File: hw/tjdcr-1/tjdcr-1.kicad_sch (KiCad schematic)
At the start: 59 parts, among them J1 Conn_Coaxial, J2 Tuning, J3 Power, J4 LO Option, J5 Volume, J6 Power, Q1 MMBT3904, Q2 MMBFJ310, Q3 MMBT3904, Q4 MMBT3904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

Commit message: Layout is progressing
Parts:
- removed Q5: MMBT3904, Package_TO_SOT_SMD:SOT-23, symbol Transistor_BJT:MMBT3904
- added H1, H2, H3, H4: MountingHole, MountingHole:MountingHole_2.5mm, symbol Mechanical:MountingHole
- added Q5: 2N3904, Package_TO_SOT_THT:TO-92_Inline, symbol Transistor_BJT:2N3904
- added TP1, TP2, TP3, TP4: TestPoint, TestPoint:TestPoint_Pad_1.5x1.5mm, symbol Connector:TestPoint
- J1: footprint Connector_Coaxial:SMA_Amphenol_901-143_Horizontal -> Connector_Coaxial:SMA_Amphenol_901-144_Vertical
- J5: footprint (none) -> Connector_PinHeader_2.54mm:PinHeader_1x03_P2.54mm_Vertical
- J6: value Power -> Speaker
- R12: value 10k -> 220
- T5: footprint (none) -> bruce-footprints:CheapAudioTransformer
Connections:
- net Audio: now also TP2.1
- net LO_I: now also TP1.1
- net at C18.2, R20.1: now also Q5.1 (E)
- net at C17.1, R16.2, R18.1: now also Q5.2 (B)
- net at C17.2, Q4.3 (C), R15.2: now also TP3.1
- net at T5.2 (AB): now also Q5.3 (C), TP4.1
- net Speaker Out: now reaches J6.1 (Pin_1), T5.4 (SB)
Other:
- moved on the sheet: J6

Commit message: Working
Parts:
- added C20: 0.47u, Capacitor_SMD:C_0805_2012Metric_Pad1.18x1.45mm_HandSolder, symbol Device:C_Small
- C11: value 0.1u -> 0.33u
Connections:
- net Audio: now also C20.1
- net GND: now also C20.2
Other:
- note added: "40m Band Pass Filter"
- note added: "Audio Diplexer"
- note added: "Audio Power Amplifier"
- note added: "Colpitts PTO/VFO"
- note added: "Connection to external gain pot."
- note added: "Double Balanced Mixer"
- note added: "J2 connection to PTO inductor (19 turns #28 on 3D printed form)"
- note added: "LO option: install jumper across J4 for internal LO, or connect external LO to pin 1 and leave pin 2 open."
- note added: "TO-92 case for better Pd"
- company: (none) -> Circuit Design by N2CQR and KK4DAS
- title: (none) -> Thomas Jefferson Direct Conversion Receiver

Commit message: Checkpoint before adding variable caps
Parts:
- added C21: 0.1u, Capacitor_SMD:C_0805_2012Metric_Pad1.18x1.45mm_HandSolder, symbol Device:C_Small
- added C22, C23: C_Variable, bruce-footprints:VCAP_GKG30086-05_SGM-L, symbol Device:C_Variable
- C11: value 0.33u -> 33u
- C13, C16, C18: footprint Capacitor_Tantalum_SMD:CP_EIA-7343-20_Kemet-V_Pad2.25x2.55mm_HandSolder -> bruce-footprints:CP_EIA-7343
- R20: value 10 -> 100
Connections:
- net GND: now also C21.1, C22.2, C23.2
- net at C2.1, C3.2, T2.4 (SB): now also C23.1
- net at C1.1, C3.1, T1.4 (SB): now also C22.1
- net at Q2.2 (S), R6.1: now also C21.2
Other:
- moved on the sheet: C1, C3, J1, R6, T1

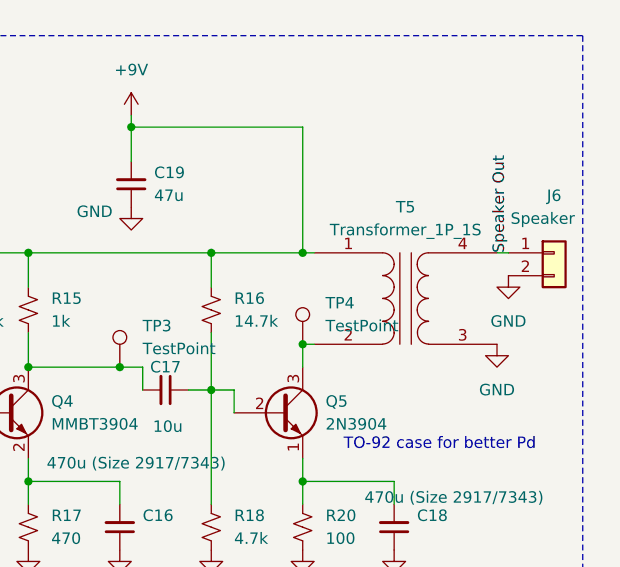
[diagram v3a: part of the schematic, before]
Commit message: Checkpoint after audio transformer change, preparing for flip of audio amp
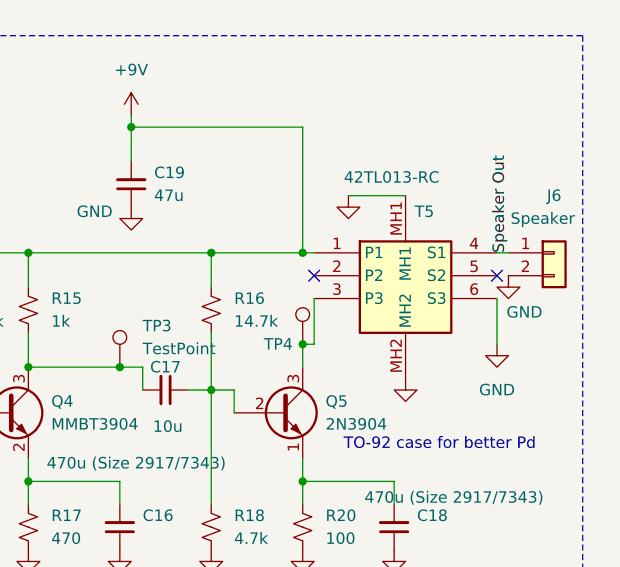
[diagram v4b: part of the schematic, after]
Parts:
- removed T5: Transformer_1P_1S, bruce-footprints:CheapAudioTransformer, symbol Device:Transformer_1P_1S
- added T5: 42TL013-RC, bruce-footprints:42TL013RC, symbol symbol-library-1:42TL013-RC
- J1: footprint Connector_Coaxial:SMA_Amphenol_901-144_Vertical -> Connector_PinHeader_2.54mm:PinHeader_1x02_P2.54mm_Vertical
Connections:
- net +9V: now also T5.1 (P1)
- net GND: now also T5.6 (S3), T5.MH1, T5.MH2
- net Speaker Out: now also T5.4 (S1)
- net at Q5.3 (C), TP4.1: now also T5.3 (P3)
- no-connect marks 0 -> 2

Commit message: Checkpoint after audio amp reverse
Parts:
- added TP5: TestPoint, TestPoint:TestPoint_Pad_1.5x1.5mm, symbol Connector:TestPoint
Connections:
- net at T2.1 (AA), T3.1 (AA): now also TP5.1
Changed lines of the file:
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@@
 	)
 	(junction
+		(at 127 43.18)
+		(diameter 0)
+		(color 0 0 0 0)
+	)
+	(junction
 		(at 210.82 38.1)
 		(diameter 0)
@@
 	(wire
 		(pts
+			(xy 124.46 43.18) (xy 127 43.18)
+		)
+		(stroke
+			(width 0)
+			(type default)
+		)
+	)
+	(wire
+		(pts
 			(xy 227.33 118.11) (xy 227.33 120.65)
 		)
@@
 	(wire
 		(pts
-			(xy 124.46 43.18) (xy 129.54 43.18)
+			(xy 133.35 102.87) (xy 144.78 102.87)
 		)
 		(stroke
@@
 	(wire
 		(pts
-			(xy 133.35 102.87) (xy 144.78 102.87)
+			(xy 144.78 125.73) (xy 144.78 128.27)
 		)
 		(stroke
@@
 	(wire
 		(pts
-			(xy 144.78 125.73) (xy 144.78 128.27)
+			(xy 196.85 43.18) (xy 198.12 43.18)
 		)
 		(stroke
@@
 	(wire
 		(pts
-			(xy 196.85 43.18) (xy 198.12 43.18)
+			(xy 85.09 105.41) (xy 88.9 105.41)
 		)
 		(stroke
@@
 	(wire
 		(pts
-			(xy 85.09 105.41) (xy 88.9 105.41)
+			(xy 194.31 102.87) (xy 204.47 102.87)
 		)
 		(stroke
@@
 	(wire
 		(pts
-			(xy 194.31 102.87) (xy 204.47 102.87)
+			(xy 68.58 129.54) (xy 68.58 130.81)
 		)
 		(stroke
@@
 	(wire
 		(pts
-			(xy 68.58 129.54) (xy 68.58 130.81)
+			(xy 66.04 105.41) (xy 66.04 107.95)
 		)
 		(stroke
@@
 	(wire
 		(pts
-			(xy 66.04 105.41) (xy 66.04 107.95)
+			(xy 127 43.18) (xy 129.54 43.18)
 		)
 		(stroke
@@
 	)
 	(rectangle
-		(start 40.005 24.765)
-		(end 240.03 71.12)
+		(start 29.845 24.765)
+		(end 125.73 71.12)
+		(stroke
+			(width 0)
+			(type dash)
+		)
+		(fill
+			(type none)
+		)
+	)
+	(rectangle
+		(start 126.365 24.765)
+		(end 243.84 71.12)
 		(stroke
 			(width 0)
@@
 					(unit 1)
 				)
+			)
+		)
+	)
+	(symbol
+		(lib_id "Connector:TestPoint")
+		(at 127 43.18 0)
+		(unit 1)
+		(exclude_from_sim no)
+		(in_bom yes)
+		(on_board yes)
+		(dnp no)
+		(fields_autoplaced yes)
+		(property "Reference" "TP5"
+			(at 129.54 38.6079 0)
+			(effects
+				(font
+					(size 1.27 1.27)
+				)
+				(justify left)
+			)
+		)
+		(property "Value" "TestPoint"
+			(at 129.54 41.1479 0)
+			(effects
+				(font
+					(size 1.27 1.27)
+				)
+				(justify left)
+			)
+		)
+		(property "Footprint" "TestPoint:TestPoint_Pad_1.5x1.5mm"
+			(at 132.08 43.18 0)
+			(effects
+				(font
+					(size 1.27 1.27)
+				)
+				(hide yes)
+			)
+		)
+		(property "Datasheet" "~"
+			(at 132.08 43.18 0)
+			(effects
+				(font
+					(size 1.27 1.27)
+				)
+				(hide yes)
+			)
+		)
+		(property "Description" "test point"
+			(at 127 43.18 0)
+			(effects
+				(font
+					(size 1.27 1.27)
+				)
+				(hide yes)
+			)
+		)
+		(pin "1"
+		)
+		(instances
+			(project "tjdcr-1"
+				(path "/4bc8412d-664e-407f-b5c0-6e2a521b9b3b"
+					(reference "TP5")
+					(unit 1)
+				)

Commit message: Ready to send this version to fab
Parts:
- C1, C2: value 160p -> 150p
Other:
- note added: "Trimmer: EW Electronics GKG30086-05 (6.5-30pF)"
- note added: "Use NP0 caps for C1/C2/C3"
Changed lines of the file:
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@@
 		)
 	)
+	(text "Trimmer: EW Electronics GKG30086-05\n(6.5-30pF)\n"
+		(exclude_from_sim no)
+		(at 85.344 62.23 0)
+		(effects
+			(font
+				(size 1.27 1.27)
+			)
+		)
+	)
 	(text "Audio Diplexer"
 		(exclude_from_sim no)
@@
 	(text "40m Band Pass Filter"
 		(exclude_from_sim no)
-		(at 90.424 34.036 0)
+		(at 81.28 27.686 0)
 		(effects
 			(font
-				(size 1.27 1.27)
+				(size 1.778 1.778)
 			)
 		)
@@
 		)
 	)
+	(text "Use NP0 caps for C1/C2/C3"
+		(exclude_from_sim no)
+		(at 68.834 37.846 0)
+		(effects
+			(font
+				(size 1.27 1.27)
+			)
+		)
+	)
 	(text "Colpitts PTO/VFO"
 		(exclude_from_sim no)
@@
 			)
 		)
-		(property "Value" "160p"
+		(property "Value" "150p"
 			(at 71.12 48.2662 0)
 			(effects
@@
 			)
 		)
-		(property "Value" "160p"
+		(property "Value" "150p"
 			(at 100.33 48.2662 0)
 			(effects

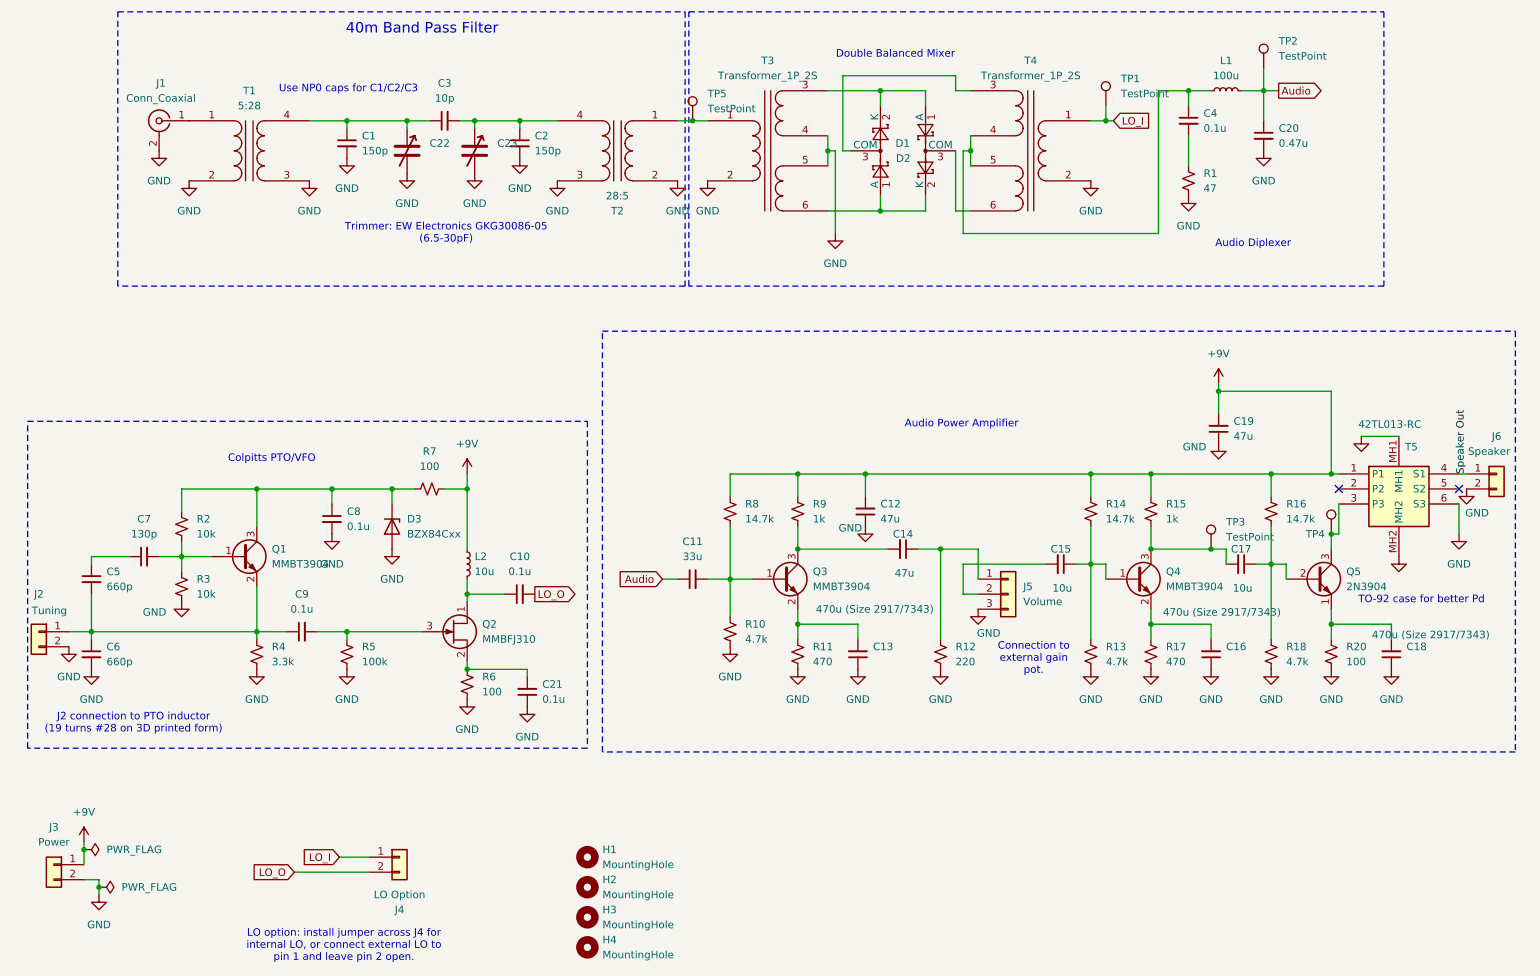
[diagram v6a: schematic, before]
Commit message: Corrected schematic error
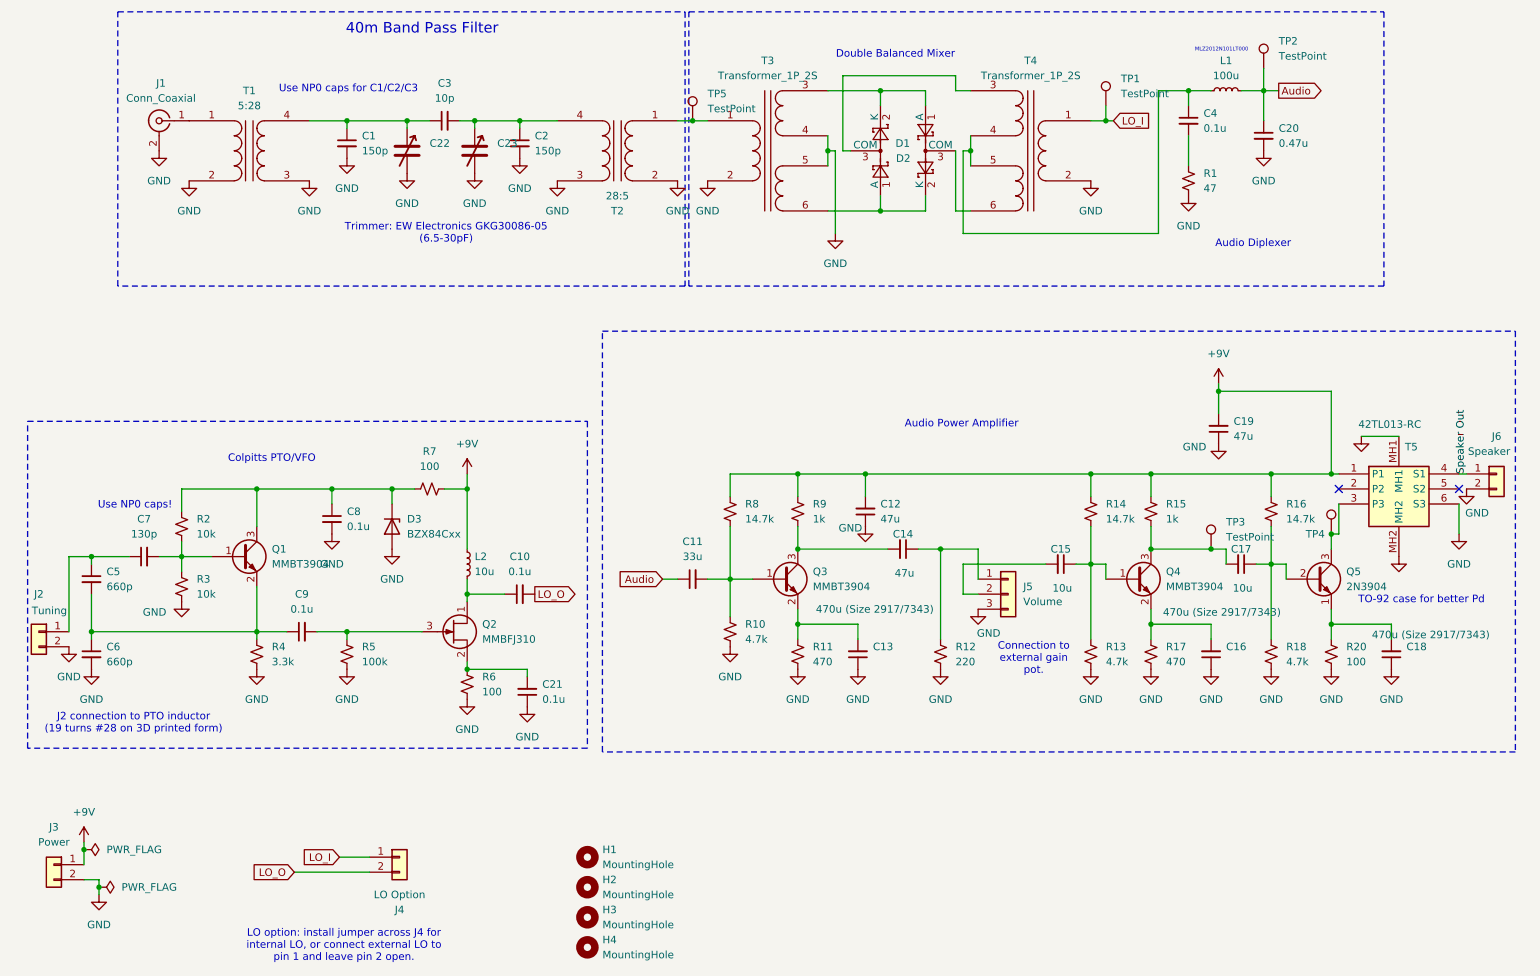
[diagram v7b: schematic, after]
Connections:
- net at C5.2, C6.1, C9.1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: no longer J2.1 (Pin_1)
- net at C5.1, C7.1: now also J2.1 (Pin_1)
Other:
- note added: "MLZ2012N101LT000"
- note added: "Use NP0 caps!"
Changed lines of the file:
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@@
+	)
+	(junction
+		(at 25.4 116.84)
+		(diameter 0)
+		(color 0 0 0 0)
 	)
 	(junction
@@
 	(wire
 		(pts
+			(xy 21.59 129.54) (xy 21.59 116.84)
+		)
+		(stroke
+			(width 0)
+			(type default)
+		)
+	)
+	(wire
+		(pts
 			(xy 156.21 106.68) (xy 156.21 102.87)
 		)
@@
 	(wire
 		(pts
+			(xy 21.59 116.84) (xy 25.4 116.84)
+		)
+		(stroke
+			(width 0)
+			(type default)
+		)
+	)
+	(wire
+		(pts
 			(xy 127 43.18) (xy 129.54 43.18)
 		)
@@
 		(pts
 			(xy 88.9 102.87) (xy 88.9 105.41)
-		)
-		(stroke
-			(width 0)
-			(type default)
-		)
-	)
-	(wire
-		(pts
-			(xy 21.59 129.54) (xy 25.4 129.54)
 		)
 		(stroke
@@
 		)
 	)
+	(text "MLZ2012N101LT000"
+		(exclude_from_sim no)
+		(at 216.408 31.242 0)
+		(effects
+			(font
+				(size 0.635 0.635)
+			)
+		)
+	)
 	(text "40m Band Pass Filter"
 		(exclude_from_sim no)
@@
 		(effects
 			(font
+				(size 1.27 1.27)
+			)
+		)
+	)
+	(text "Use NP0 caps!"
+		(exclude_from_sim no)
+		(at 32.766 108.204 0)
+		(effects
+			(font

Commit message: Sent to JLCPCB
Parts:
- D3: value BZX84Cxx -> 8.2V BZX84Cxx (BZX84C8V2LT1G)
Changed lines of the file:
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@@
 			)
 		)
-		(property "Value" "BZX84Cxx"
+		(property "Value" "8.2V BZX84Cxx (BZX84C8V2LT1G)"
 			(at 78.74 113.0299 90)
 			(effects
